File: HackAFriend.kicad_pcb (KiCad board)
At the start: 2 copper layers, 135 x 59 mm, 103 parts, among them J1 PRT-14417, J10 Conn_01x16, J11 USB_C_Receptacle_USB2.0_16P, J3 Conn_01x02, J4 Conn_01x02, J5 Conn_01x02, J7 Conn_01x02, J8 Conn_01x12, J9 Conn_01x02, P1 TC2050-IDC, SW1 GP0115ACCG30, SW10 SPST_BTN_A, SW11 SPST_BTN_X, SW12 SPST_BTN_Y, SW2 SW_SPST, SW3 SPST_DPAD_LEFT, SW4 SPST_BTN_SELECT, SW5 SPST_DPAD_DOWN, SW6 SPST_DPAD_RIGHT, SW7 SPST_DPAD_UP, SW8 SPST_DPAD_START, SW9 SPST_BTN_B, U2 DRV2605LDGS, U3 W25Q64JVSSIQ, U4 MCP23017_ML, U6 BQ24072RGT, U7 MAX98357A, U8 NJM2884U1-33-TE1, U9 MDBT50Q-1MV2, Y1 ABS06-32.768KHZ-1-T

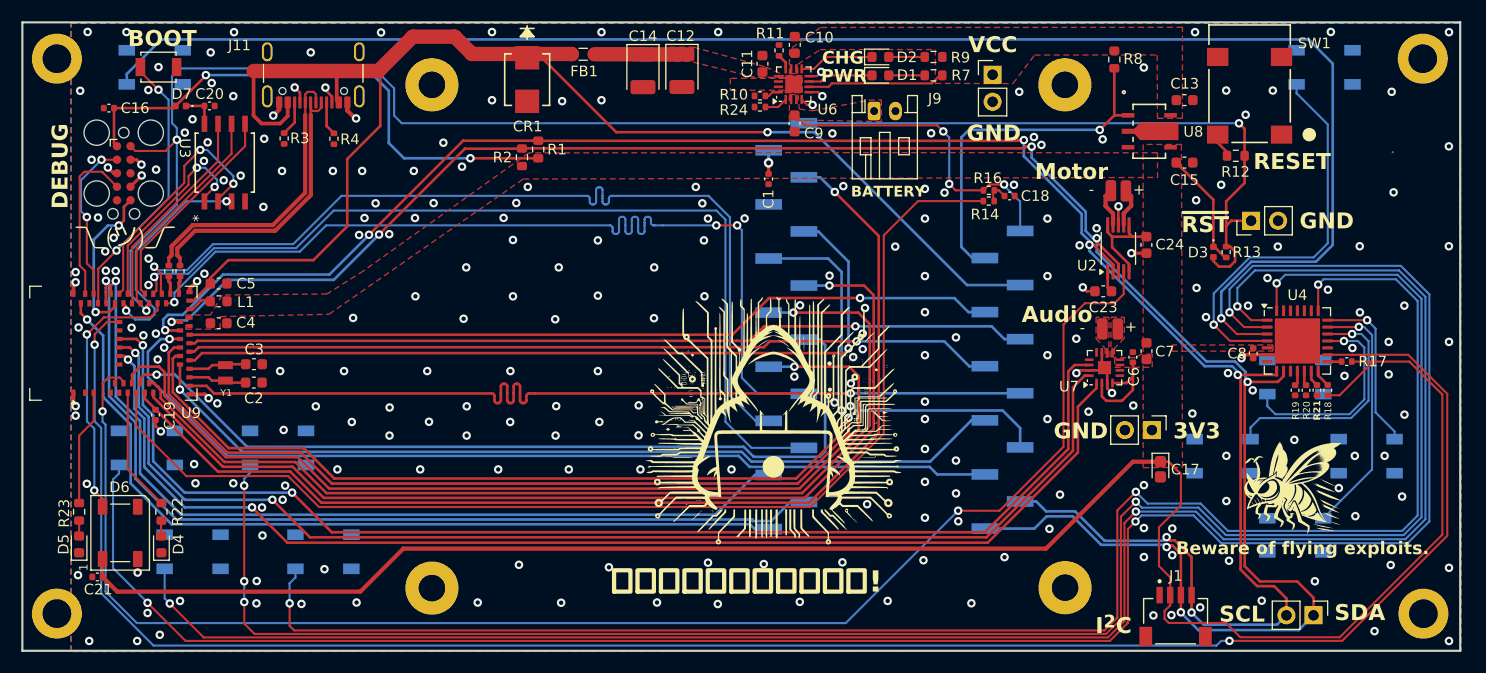
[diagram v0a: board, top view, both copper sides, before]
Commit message: Changed reset button, upgrade to new KiCad
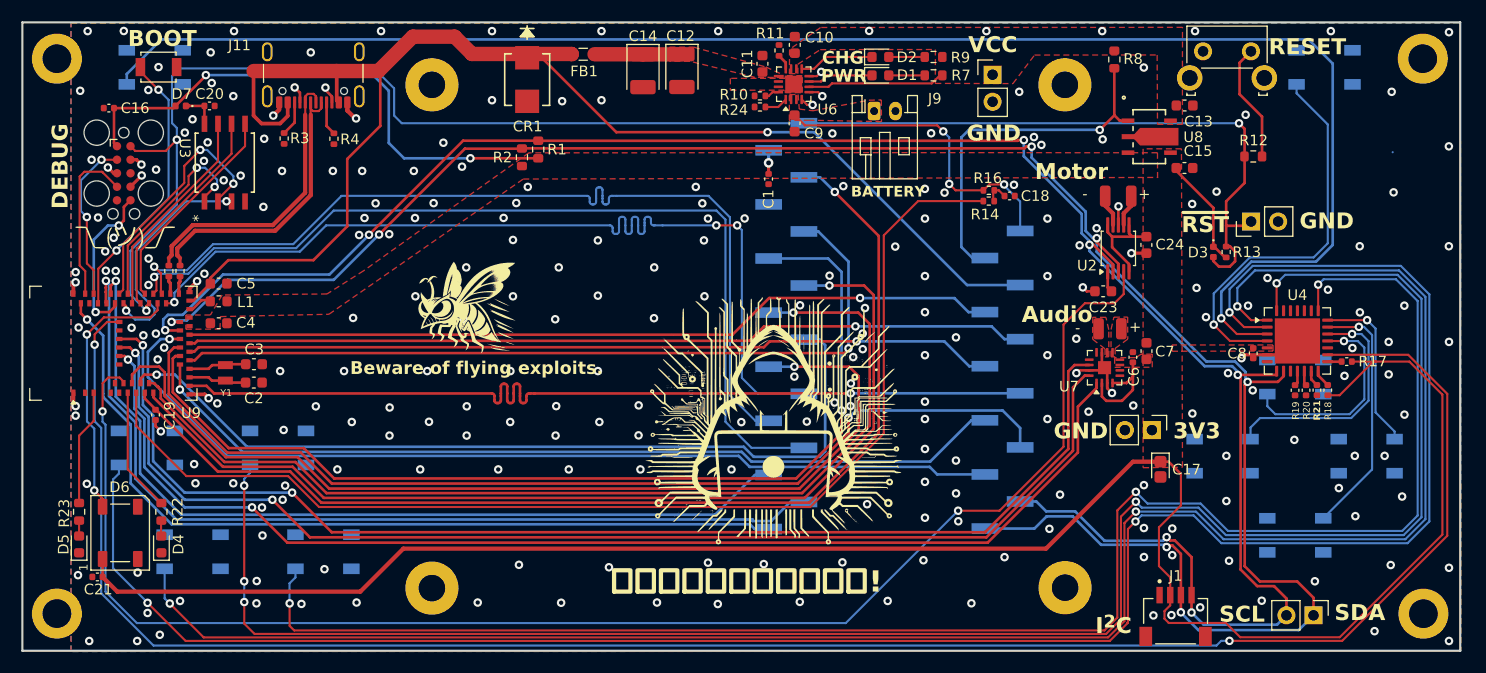
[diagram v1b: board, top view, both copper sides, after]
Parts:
- SW1: value GP0115ACCG30 -> ~; footprint GP0115ACCG30:SW_GP0115ACCG30_NKK -> Button_Switch_THT:SW_SPST_Omron_B3F-315x_Angled
- moved G*** 79.4 mm to (123.0, 88.2)
- moved SW1 4.63 mm to (191.9, 64.2), turned to 0 degrees
- moved G*** 3.64 mm to (103.1, 86.5)
- moved G*** 1.71 mm to (190.9, 63.1)
- moved R12 1.64 mm to (196.6, 74.1), turned to 180 degrees
- moved LPAD_OUT-1 0.74 mm to (182.7, 77.8)
- moved LPAD_OUT+1 0.71 mm to (185.2, 77.8)
- moved C13 0.51 mm to (190.2, 69.3)
- moved U8 0.51 mm to (186.9, 72.2)
- moved C15 0.51 mm to (190.2, 75.2)
- moved LPAD_OUT-2 0.36 mm to (182.1, 90.2)
- moved LPAD_OUT+2 0.33 mm to (184.2, 90.2)
- moved J7 0.07 mm to (196.4, 80.2)
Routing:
- net Net-(R12-Pad1): track 2.40 -> 11.2 mm
- net /Human Interfaces/MOTOR_OUT-: track 3.72 -> 3.01 mm
- net /Human Interfaces/MOTOR_OUT+: track 3.70 -> 2.99 mm
- net +3V3: track 267.2 -> 266.7 mm
- net GND: vias 257 -> 259

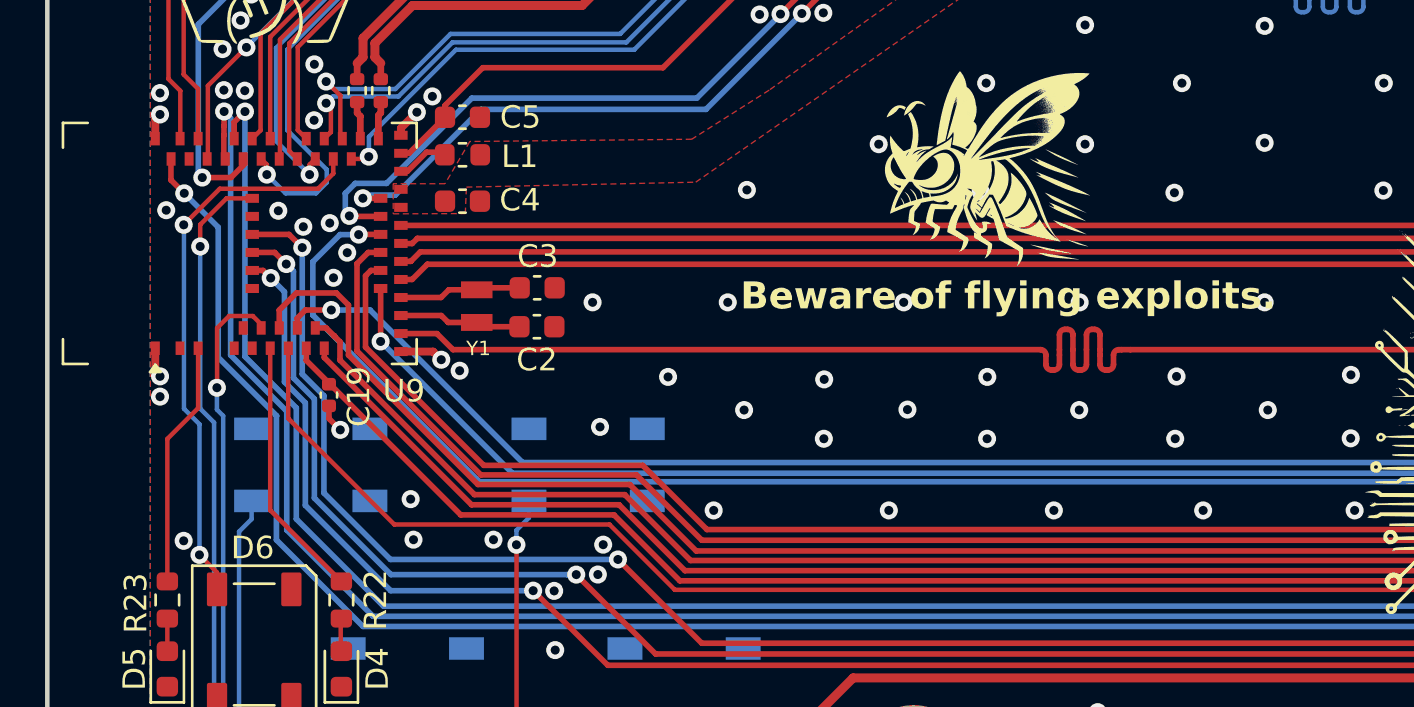
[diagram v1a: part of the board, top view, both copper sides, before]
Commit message: Added MP part number fields to schematic and PCB design,
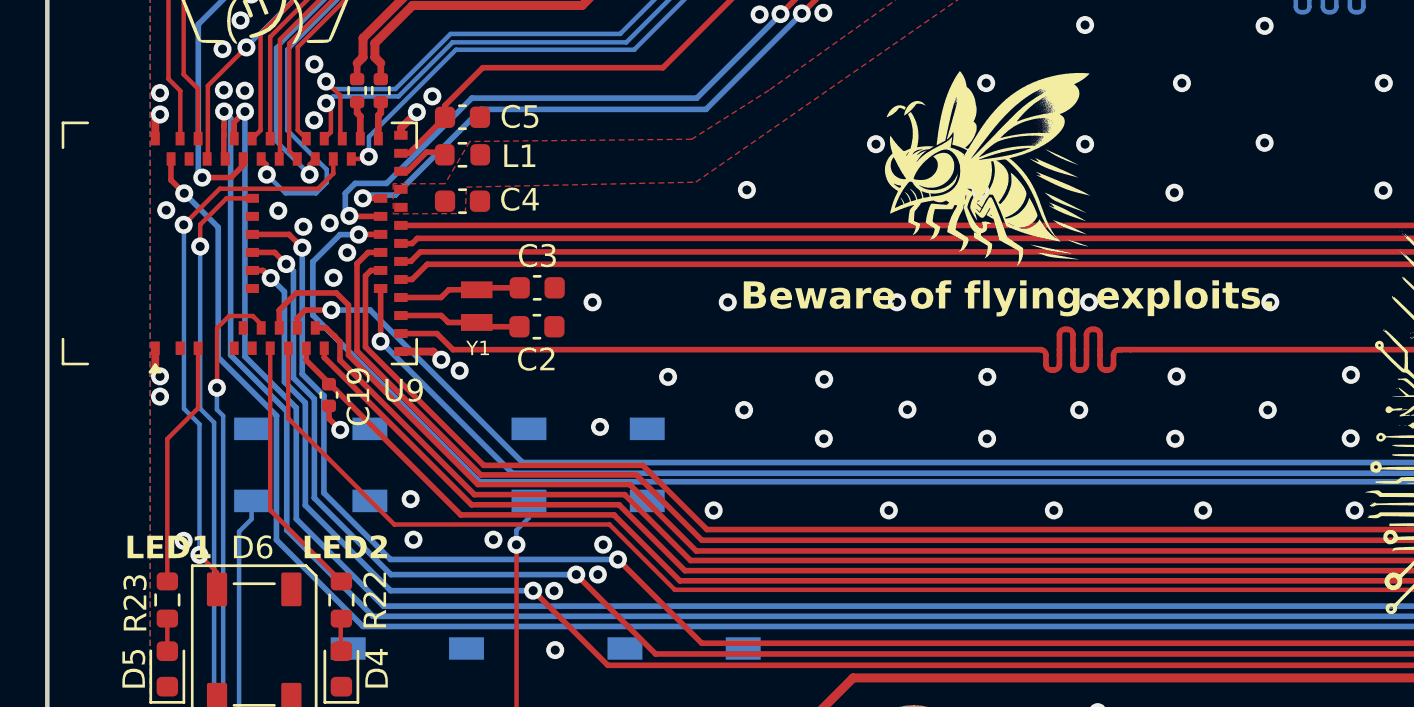
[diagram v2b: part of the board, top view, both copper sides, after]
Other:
- board text added: "Hack-A-Friend Version 0.9"
- board text added: "LED1"
- board text added: "LED2"
- board text removed: "Hack-A-Friend Version 1.0"
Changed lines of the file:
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@@
 			)
 		)
+		(property "MP" "B3F-3155"
+			(at 0 0 0)
+			(unlocked yes)
+			(layer "F.Fab")
+			(hide yes)
+			(effects
+				(font
+					(size 1 1)
+					(thickness 0.15)
+				)
+			)
+		)
 		(sheetname "/Power/")
 		(sheetfile "power.kicad_sch")
@@
 			)
 		)
+		(property "MP" "DRV2605LDGSR"
+			(at 0 0 90)
+			(unlocked yes)
+			(layer "F.Fab")
+			(hide yes)
+			(effects
+				(font
+					(size 1 1)
+					(thickness 0.15)
+				)
+			)
+		)
 		(property ki_fp_filters "VSSOP*3x3mm*P0.5mm*")
 		(sheetname "/Human Interfaces/")
@@
 		)
 	)
+	(gr_text "LED2"
+		(at 92.351905 105.7 0)
+		(layer "F.SilkS")
+		(effects
+			(font
+				(size 1 1)
+				(thickness 0.2)
+				(bold yes)
+			)
+			(justify left bottom)
+		)
+	)
 	(gr_text "SCL"
 		(at 193.4198 117.93 0)
@@
 		)
 	)
+	(gr_text "LED1"
+		(at 84.493005 105.7 0)
+		(layer "F.SilkS")
+		(effects
+			(font
+				(size 1 1)
+				(thickness 0.2)
+				(bold yes)
+			)
+			(justify left bottom)
+		)
+	)
 	(gr_text "3V3"
 		(at 189.1048 100.72 0)
@@
 		)
 	)
-	(gr_text "Hack-A-Friend\nVersion 1.0"
+	(gr_text "Hack-A-Friend\nVersion 0.9"
 		(at 108.9848 119.88 0)
 		(layer "B.SilkS")
@@
 	)
 	(via
-		(at 119.0698 94.22)
+		(at 118.769561 94.216989)
 		(size 0.8)
 		(drill 0.4)
@@
 	)
 	(via
-		(at 117.9598 87.2)
+		(at 117.838436 87.199811)
 		(size 0.8)
 		(drill 0.4)
@@
 	)
 	(via
-		(at 135.0898 94.22)
+		(at 135.340897 94.216989)
 		(size 0.8)
 		(drill 0.4)
@@
 	)
 	(via
-		(at 126.8798 94.22)
+		(at 127.298131 94.216989)
 		(size 0.8)
 		(drill 0.4)
